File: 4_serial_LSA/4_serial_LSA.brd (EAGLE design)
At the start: 52 x 40.7 mm, 8 parts, among them J1 ED555/2DS

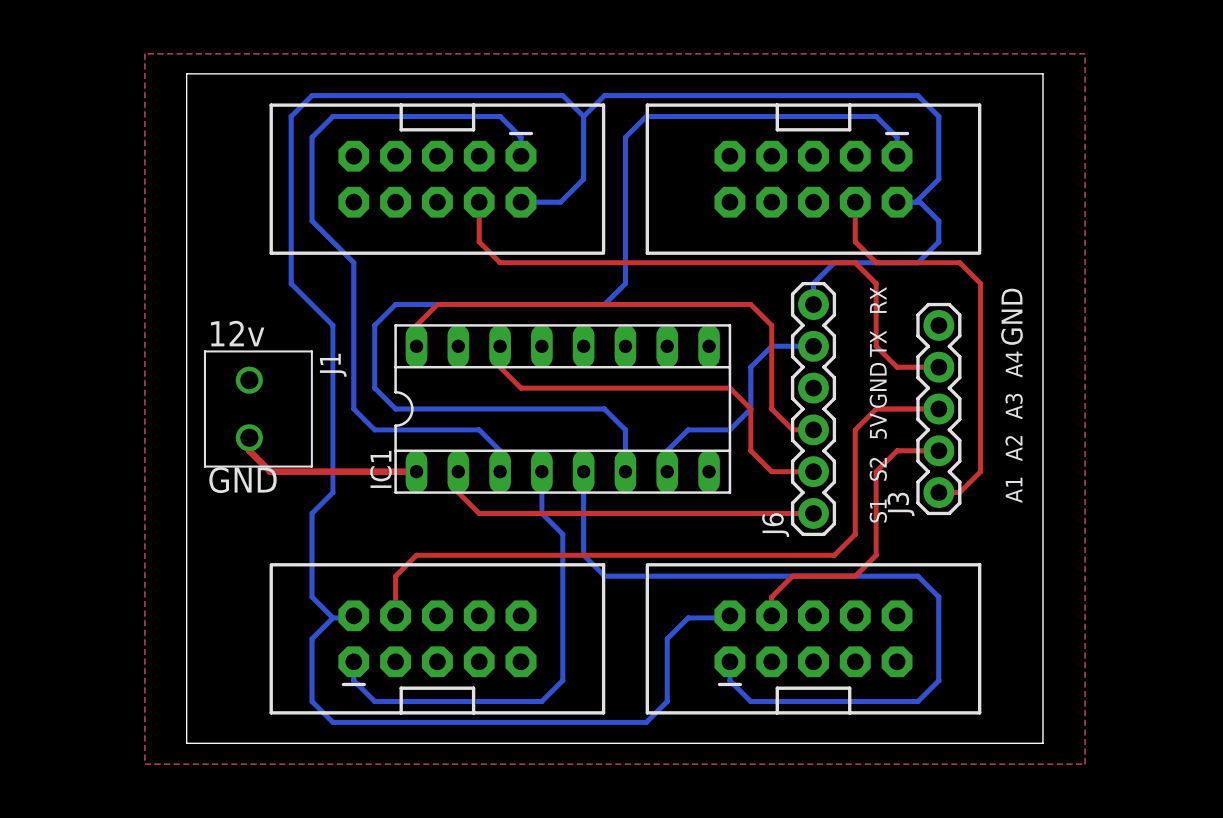
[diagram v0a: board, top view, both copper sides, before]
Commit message: add the new molex connetor
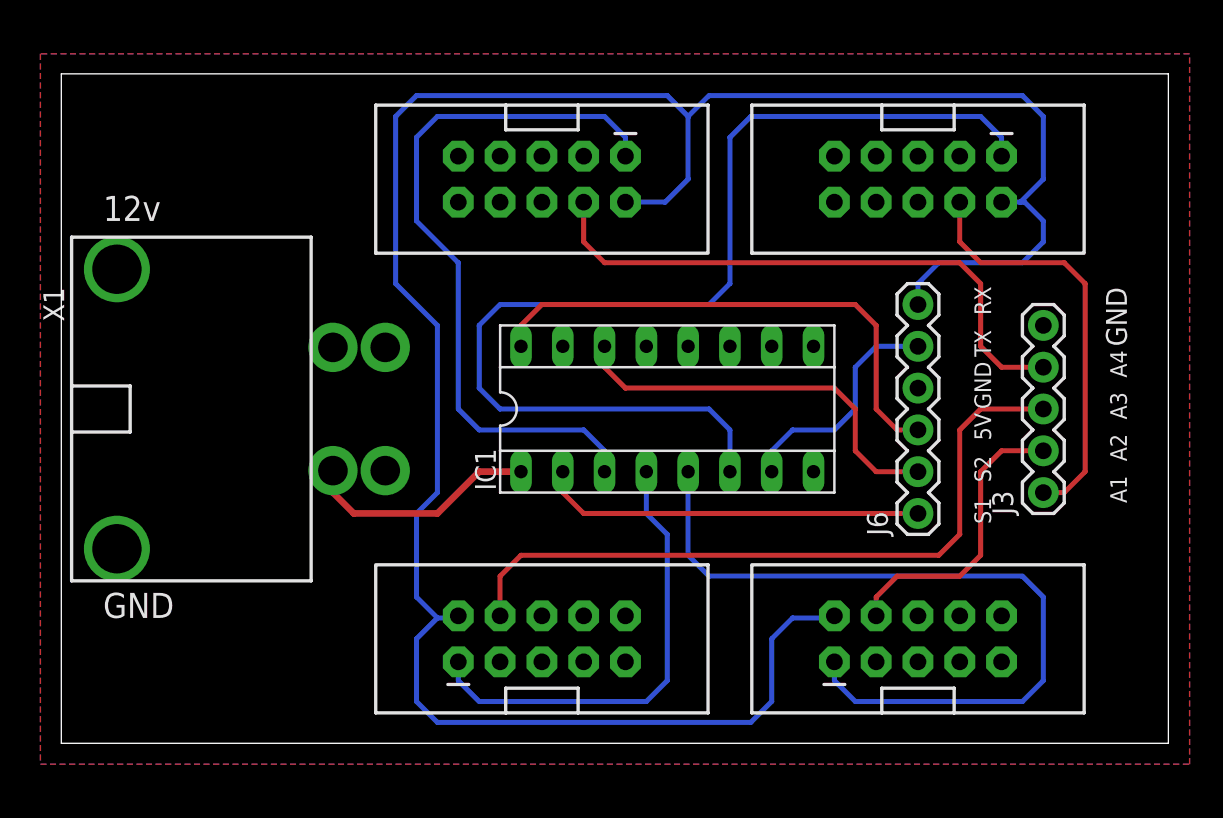
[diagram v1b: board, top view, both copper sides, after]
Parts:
- removed J1: ED555/2DS, DC_LOAD_AU:ED555/2DS
- added X1: 43160-3102, con-molex:43160-XX02
- moved IC1 6.35 mm to (30.5, 20.3)
- moved J3 6.35 mm to (53.3, 15.2)
- moved J6 6.35 mm to (45.7, 14.0)
- moved LSA1 6.35 mm to (45.7, 34.3)
- moved LSA2 6.35 mm to (45.7, 6.35)
- moved LSA3 6.35 mm to (22.9, 6.35)
- moved LSA4 6.35 mm to (22.9, 34.3)
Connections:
- net 12V: now also X1.1@1; no longer J1.1
- net GND: now also X1.2@1; no longer J1.2
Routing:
- net GND: track 11.5 -> 14.3 mm
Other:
- board size 52 x 40.7 mm -> 67.3 x 40.7 mm

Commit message: minor changes, can be ignored
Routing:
- net GND: track 14.3 -> 1.33 mm
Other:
- board size 67.3 x 40.7 mm -> 67.3 x 43.2 mm
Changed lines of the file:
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@@
 <board>
 <plain>
-<wire x1="-6.35" y1="0" x2="60.94" y2="0" width="0" layer="20"/>
-<wire x1="60.94" y1="0" x2="60.94" y2="40.691" width="0" layer="20"/>
-<wire x1="60.94" y1="40.691" x2="-6.35" y2="40.691" width="0" layer="20"/>
-<wire x1="-6.35" y1="40.691" x2="-6.35" y2="0" width="0" layer="20"/>
+<wire x1="-6.35" y1="-1.27" x2="60.94" y2="-1.27" width="0" layer="20"/>
+<wire x1="60.94" y1="-1.27" x2="60.94" y2="41.961" width="0" layer="20"/>
+<wire x1="60.94" y1="41.961" x2="-6.35" y2="41.961" width="0" layer="20"/>
+<wire x1="-6.35" y1="41.961" x2="-6.35" y2="-1.27" width="0" layer="20"/>
 <text x="-3.81" y="31.75" size="1.524" layer="25">12v</text>
 <text x="-3.81" y="7.62" size="1.524" layer="25">GND</text>
@@
 <contactref element="IC1" pad="15"/>
 <polygon width="0.3048" layer="16" isolate="0.3048">
-<vertex x="-7.62" y="41.91"/>
-<vertex x="-7.62" y="-1.27"/>
-<vertex x="62.23" y="-1.27"/>
-<vertex x="62.23" y="41.91"/>
+<vertex x="-7.62" y="43.18"/>
+<vertex x="-7.62" y="-2.54"/>
+<vertex x="62.23" y="-2.54"/>
+<vertex x="62.23" y="43.18"/>
 </polygon>
 <contactref element="X1" pad="2@1"/>
-<wire x1="21.59" y1="16.51" x2="19.05" y2="16.51" width="0.4064" layer="1"/>
-<wire x1="16.51" y1="13.97" x2="11.43" y2="13.97" width="0.4064" layer="1"/>
-<wire x1="11.43" y1="13.97" x2="10.16" y2="15.24" width="0.4064" layer="1"/>
 <wire x1="10.16" y1="15.24" x2="10.16" y2="16.575" width="0.4064" layer="1"/>
-<wire x1="19.05" y1="16.51" x2="16.51" y2="13.97" width="0.4064" layer="1"/>
 </signal>
 <signal name="12V">
 <contactref element="LSA3" pad="9"/>
-<polygon width="0.3048" layer="1" isolate="0.3048">
-<vertex x="-7.62" y="41.91"/>
-<vertex x="-7.62" y="-1.27"/>
-<vertex x="62.23" y="-1.27"/>
-<vertex x="62.23" y="41.91"/>
-</polygon>
 <contactref element="LSA4" pad="9"/>
 <contactref element="LSA1" pad="9"/>
 <contactref element="LSA2" pad="9"/>
 <contactref element="X1" pad="1@1"/>
+<polygon width="0.1524" layer="1">
+<vertex x="-7.62" y="43.18"/>
+<vertex x="-7.62" y="-2.54"/>
+<vertex x="62.23" y="-2.54"/>
+<vertex x="62.23" y="43.18"/>
+</polygon>
 </signal>
 <signal name="RX">
